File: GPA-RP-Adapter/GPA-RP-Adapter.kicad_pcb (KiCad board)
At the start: 4 copper layers, 60 x 56 mm, 23 parts, among them J1 PWR_Fan, J11 Conn_02x03_Odd_Even, J12 Analog In 0, J13 Analog In 1, J16 Analog Out 0, J17 Analog Out 1, J2 Conn_Coaxial, J3 Conn_01x02, J4 RJ45, J5 Conn_01x03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

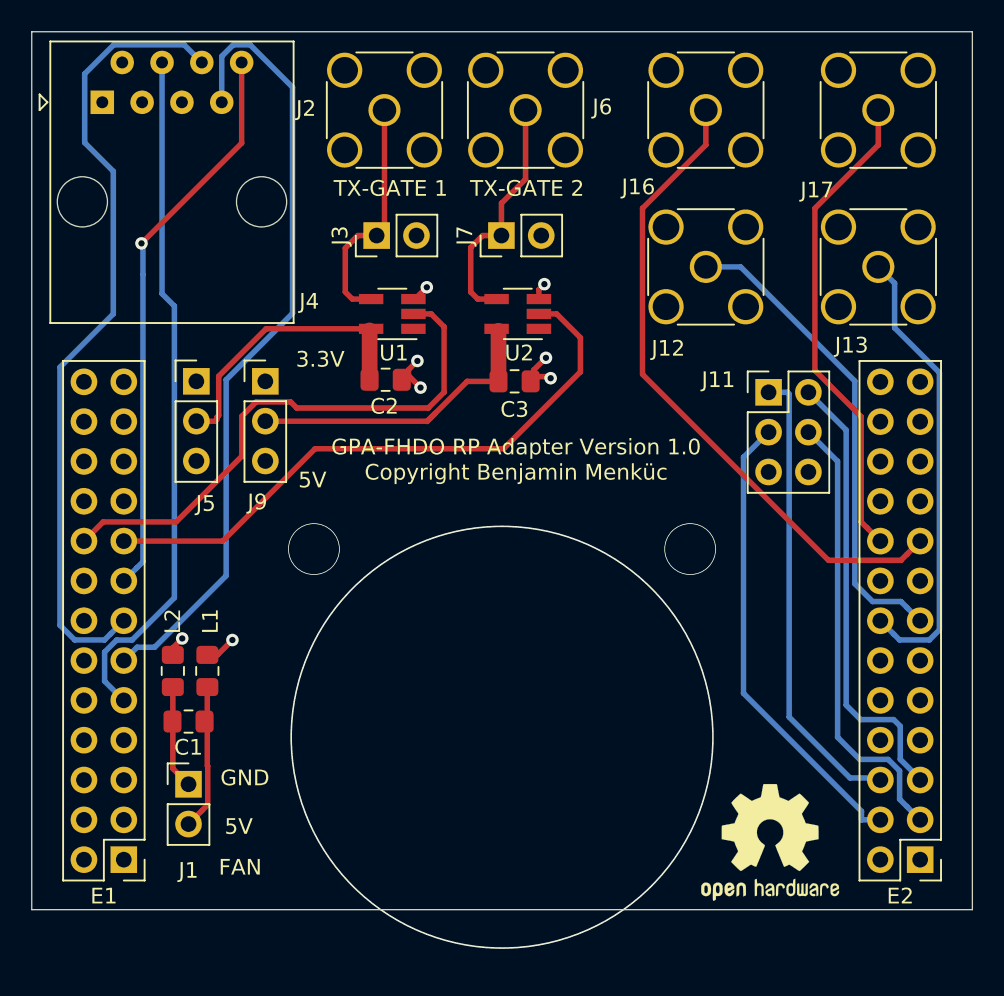
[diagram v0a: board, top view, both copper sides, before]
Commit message: fixed some errors in layout - rotated rj45 connector - connected the 5V layer properly
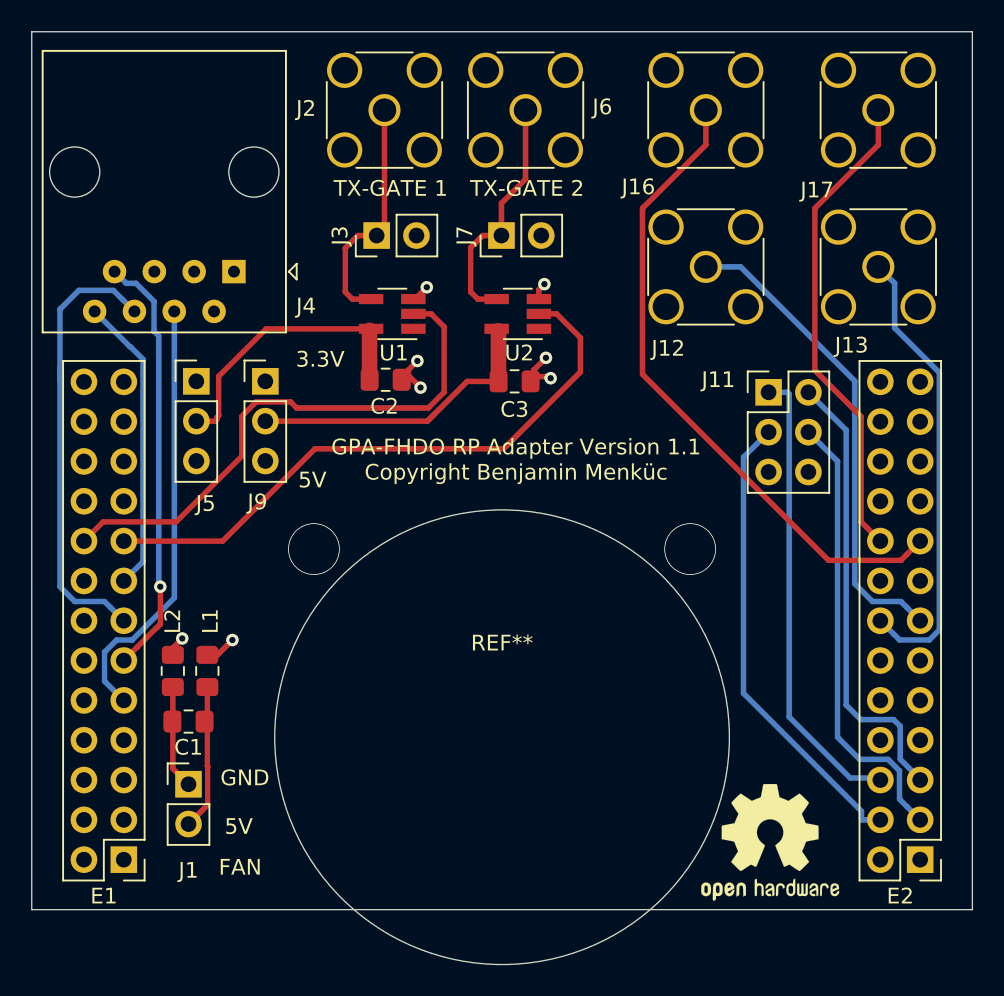
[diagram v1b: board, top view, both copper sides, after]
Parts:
- added REF**: MountingHole_5mm, MountingHole:MountingHole_5mm, F.Cu at (130.0, 105.0)
- moved J4 13.7 mm to (112.9, 75.3), turned to 180 degrees
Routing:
- net /CS: track 50.6 -> 27.4 mm, vias 0 -> 1
- net /MO: track 51.0 -> 29.3 mm
- net /MI: track 36.3 -> 19.0 mm, vias 1 -> 0
- net /CLK: track 43.9 -> 26.9 mm
- net (no net): vias 3 -> 2
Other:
- board text added: "GPA-FHDO RP Adapter Version 1.1 Copyright Benjamin Menküc"
- board text removed: "GPA-FHDO RP Adapter Version 1.0 Copyright Benjamin Menküc"
